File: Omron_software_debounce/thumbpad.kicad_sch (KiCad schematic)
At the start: 19 parts, among them J1 Conn_01x06, SW1 D2LS-2120M, SW2 D2LS-2120M, SW3 D2LS-2120M, SW4 D2LS-2120M

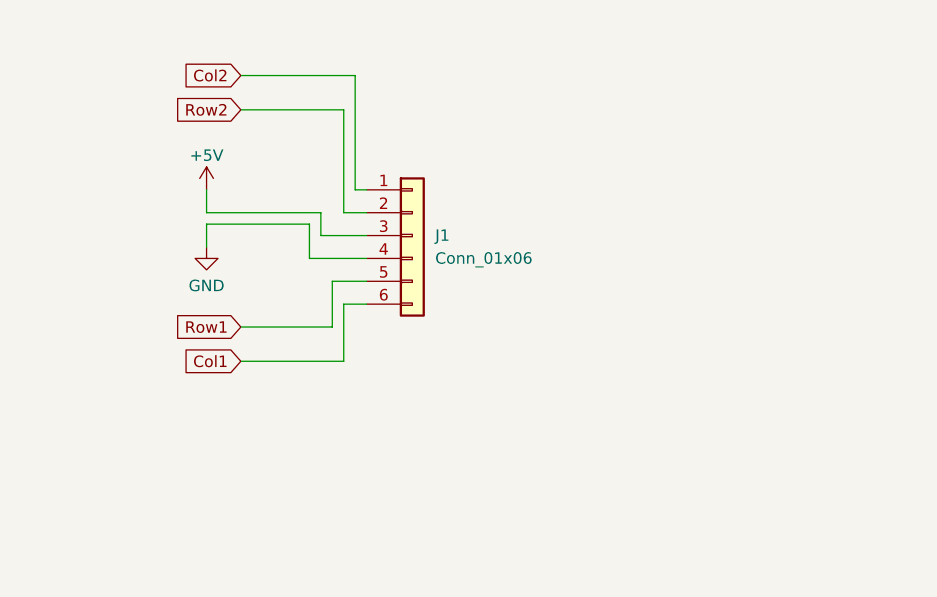
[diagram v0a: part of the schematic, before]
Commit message: Added pth pads for hand solder/pin headers
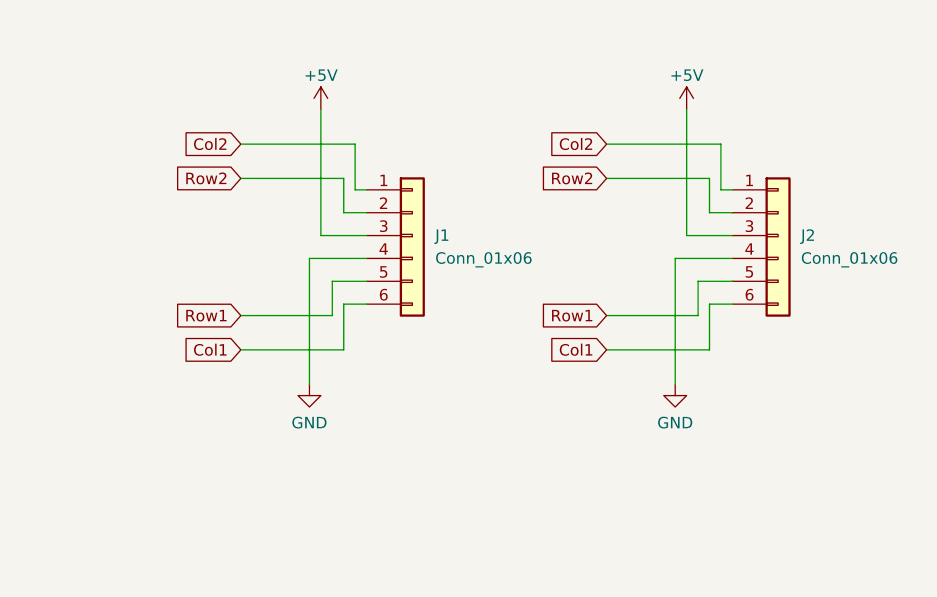
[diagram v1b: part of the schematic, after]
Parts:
- added J2: Conn_01x06, My_Library:pads_connector_0.1mm, symbol Connector_Generic:Conn_01x06
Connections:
- net +5V: now also J2.3 (Pin_3)
- net Col1: now also J2.6 (Pin_6)
- net Col2: now also J2.1 (Pin_1)
- net GND: now also J2.4 (Pin_4)
- net Row1: now also J2.5 (Pin_5)
- net Row2: now also J2.2 (Pin_2)
